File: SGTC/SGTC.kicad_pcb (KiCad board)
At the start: 2 copper layers, 110.5 x 62.6 mm, 9 parts, among them J1 Conn_01x08_Pin

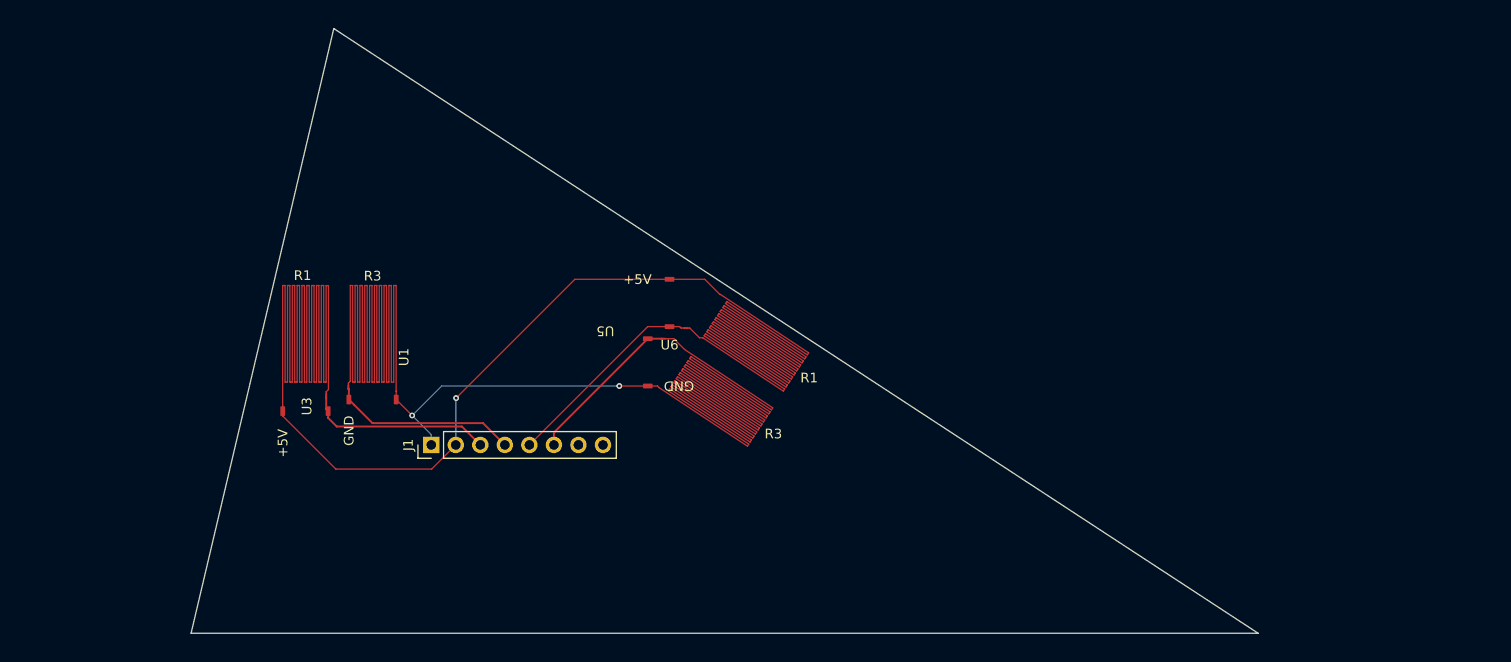
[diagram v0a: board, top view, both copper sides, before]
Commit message: fin center draft
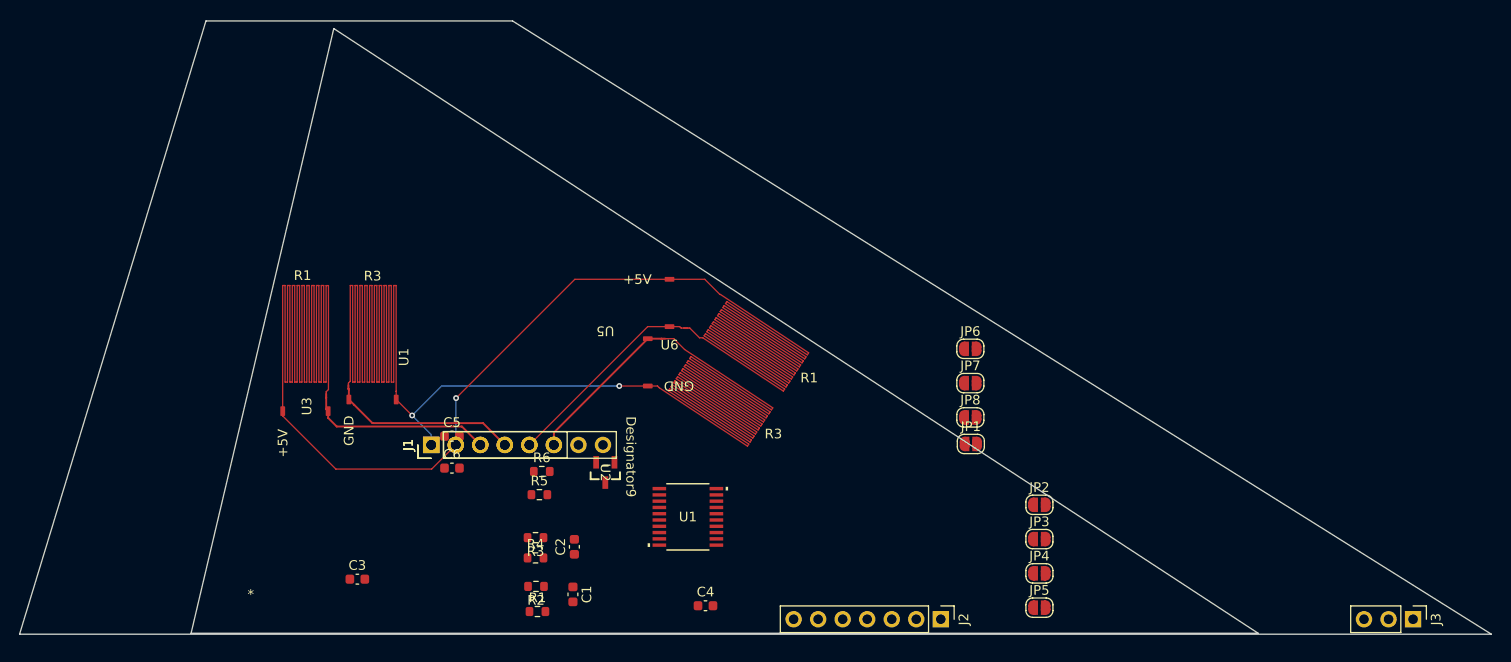
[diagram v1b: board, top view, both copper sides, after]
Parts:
- added C1: 10 nF, Capacitor_SMD:C_0603_1608Metric, F.Cu at (119.6, 120.8)
- added C2: 10 nF, Capacitor_SMD:C_0603_1608Metric, F.Cu at (119.8, 115.8)
- added C3: 10 nF, Capacitor_SMD:C_0603_1608Metric, F.Cu at (97.3, 119.2)
- added C4: 220 nF, Capacitor_SMD:C_0603_1608Metric, F.Cu at (133.3, 122.0)
- added C5: 1 uF, Capacitor_SMD:C_0603_1608Metric, F.Cu at (107.1, 104.4)
- added C6: 1 uF, Capacitor_SMD:C_0603_1608Metric, F.Cu at (107.1, 107.7)
- added J1: Conn_01x06_Pin, Connector_PinHeader_2.54mm:PinHeader_1x06_P2.54mm_Vertical, F.Cu at (104.9, 105.3)
- added J2: Conn_01x07_Pin, Connector_PinHeader_2.54mm:PinHeader_1x07_P2.54mm_Vertical, F.Cu at (157.7, 123.3)
- added J3: Conn_01x03_Pin, Connector_PinHeader_2.54mm:PinHeader_1x03_P2.54mm_Vertical, F.Cu at (206.6, 123.3)
- added JP1: SolderJumper_2_Open, Jumper:SolderJumper-2_P1.3mm_Open_RoundedPad1.0x1.5mm, F.Cu at (160.8, 105.2)
- added JP2: SolderJumper_2_Open, Jumper:SolderJumper-2_P1.3mm_Open_RoundedPad1.0x1.5mm, F.Cu at (167.9, 111.5)
- added JP3: SolderJumper_2_Open, Jumper:SolderJumper-2_P1.3mm_Open_RoundedPad1.0x1.5mm, F.Cu at (167.9, 115.0)
- added JP4: SolderJumper_2_Open, Jumper:SolderJumper-2_P1.3mm_Open_RoundedPad1.0x1.5mm, F.Cu at (167.9, 118.6)
- added JP5: SolderJumper_2_Open, Jumper:SolderJumper-2_P1.3mm_Open_RoundedPad1.0x1.5mm, F.Cu at (167.9, 122.2)
- added JP6: SolderJumper_2_Open, Jumper:SolderJumper-2_P1.3mm_Open_RoundedPad1.0x1.5mm, F.Cu at (160.8, 95.3)
- added JP7: SolderJumper_2_Open, Jumper:SolderJumper-2_P1.3mm_Open_RoundedPad1.0x1.5mm, F.Cu at (160.8, 98.9)
- added JP8: SolderJumper_2_Open, Jumper:SolderJumper-2_P1.3mm_Open_RoundedPad1.0x1.5mm, F.Cu at (160.8, 102.5)
- added R1: 10 k, Resistor_SMD:R_0603_1608Metric, F.Cu at (115.9, 122.5)
- added R2: 10 k, Resistor_SMD:R_0603_1608Metric, F.Cu at (115.8, 120.0)
- added R3: 10 k, Resistor_SMD:R_0603_1608Metric, F.Cu at (115.7, 114.9)
- added R4: 10 k, Resistor_SMD:R_0603_1608Metric, F.Cu at (115.7, 117.0)
- added R5: 10 k, Resistor_SMD:R_0603_1608Metric, F.Cu at (116.1, 110.5)
- added R6: 10 k, Resistor_SMD:R_0603_1608Metric, F.Cu at (116.4, 108.0)
- added U1: ADS131M03QPWRQ1, FinLib:ADS131M03, F.Cu at (131.5, 112.8)
- added U2: TMP235A4DBZR, FinLib:TMP235A4DBZR, F.Cu at (122.9, 108.2)
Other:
- board size 110.5 x 62.6 mm -> 152.4 x 63.5 mm

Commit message: strain gauge fix
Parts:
- removed C1, C2, C3: 10 nF, Capacitor_SMD:C_0603_1608Metric
- removed C4: 220 nF, Capacitor_SMD:C_0603_1608Metric
- removed C5, C6: 1 uF, Capacitor_SMD:C_0603_1608Metric
- removed J2: Conn_01x07_Pin, Connector_PinHeader_2.54mm:PinHeader_1x07_P2.54mm_Vertical
- removed J3: Conn_01x03_Pin, Connector_PinHeader_2.54mm:PinHeader_1x03_P2.54mm_Vertical
- removed JP1, JP2, JP3, JP4, JP5, JP6, JP7, JP8: SolderJumper_2_Open, Jumper:SolderJumper-2_P1.3mm_Open_RoundedPad1.0x1.5mm
- removed R1, R2, R3, R4, R5, R6: 10 k, Resistor_SMD:R_0603_1608Metric
- removed the REF** at (128.8, 94.3)
- removed the REF** at (96.3, 99.4)
- removed the REF** at (94.0, 100.3)
- removed the REF** at (131.2, 93.2)
- removed U1: ADS131M03QPWRQ1, FinLib:ADS131M03
- removed U1: ~, Library:StrainGaugeGND
- removed U2: TMP235A4DBZR, FinLib:TMP235A4DBZR
- removed the U5 at (127.3, 94.3)
- removed the U6 at (129.6, 95.5)
- added REF**: NetTie-2_SMD_Pad0.1mm, Library:NetTie-2_SMD_Pad0.1mm, F.Cu at (188.8, 87.7)
- added REF**: NetTie-2_SMD_Pad0.1mm, Library:NetTie-2_SMD_Pad0.1mm, F.Cu at (155.4, 91.8)
- added REF**: NetTie-2_SMD_Pad0.1mm, Library:NetTie-2_SMD_Pad0.1mm, F.Cu at (131.5, 93.6)
- added REF**: NetTie-2_SMD_Pad0.1mm, Library:NetTie-2_SMD_Pad0.1mm, F.Cu at (153.9, 93.4)
- added REF**: NetTie-2_SMD_Pad0.1mm, Library:NetTie-2_SMD_Pad0.1mm, F.Cu at (130.0, 95.2)
- added REF**: NetTie-2_SMD_Pad0.1mm, Library:NetTie-2_SMD_Pad0.1mm, F.Cu at (96.5, 99.3)
- added REF**: NetTie-2_SMD_Pad0.1mm, Library:NetTie-2_SMD_Pad0.1mm, F.Cu at (94.3, 99.3)
- added REF**: NetTie-2_SMD_Pad0.1mm, Library:NetTie-2_SMD_Pad0.1mm, F.Cu at (191.1, 87.7)
- added U3: ~, Library:StrainGaugeGND, F.Cu at (192.5, 86.1)
- added U5: ~, Library:StrainGaugeGND, F.Cu at (157.9, 92.2)
- added U5: ~, Library:StrainGaugeGND, F.Cu at (98.0, 100.9)
- added U5: ~, Library:StrainGaugeGND, F.Cu at (187.4, 86.1)
- added U5: ~, Library:StrainGaugeGND, F.Cu at (127.5, 94.8)
- added U6: ~, Library:StrainGaugeV, F.Cu at (154.3, 95.6)
- added U6: ~, Library:StrainGaugeV, F.Cu at (131.1, 91.4)
- J1: value Conn_01x08_Pin -> Conn_01x06_Pin; footprint Connector_PinHeader_2.54mm:PinHeader_1x08_P2.54mm_Vertical -> Connector_PinHeader_2.54mm:PinHeader_1x06_P2.54mm_Vertical
- U3: footprint Library:StrainGaugeV -> Library:StrainGaugeGND
- moved J1 79.1 mm to (180.5, 81.7), turned to -90 degrees
- moved U3 4.05 mm to (92.9, 100.8)
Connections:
- J1 pad 1: GAUGE1_IN_N -> A1_IN_N
- J1 pad 2: GAUGE1_IN_P -> A1_IN_P
- J1 pad 4: TMP_IN_N -> GND
- J1 pad 5: GAUGE2_IN_N -> A2_IN_N
- J1 pad 6: GAUGE2_IN_P -> A2_IN_P
- J1 pad 1: GND -> A1_IN_N
- J1 pad 2: +5V -> A1_IN_P
- J1 pad 3: A1_IN_P -> +3.3V
- J1 pad 4: A1_IN_N -> GND
- J1 pad 5: A2_IN_P -> A2_IN_N
- J1 pad 6: A2_IN_N -> A2_IN_P
- U3 pad 1: +5V -> +3.3V
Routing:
- net +3.3V: track 0.00 -> 934.7 mm
- net +5V: track 476.3 -> 0.00 mm, vias 1 -> 0
- net GND: track 448.8 -> 829.4 mm, vias 2 -> 0
- net A2_IN_N: track 16.4 -> 43.8 mm
- net A2_IN_P: track 21.1 -> 43.1 mm, vias 0 -> 2
- net A1_IN_P: track 19.1 -> 33.5 mm
- net A1_IN_N: track 19.2 -> 26.9 mm
- added copper zone on B.Cu, net GND
- added copper zone on F.Cu, net GND
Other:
- board size 152.4 x 63.5 mm -> 125.3 x 62.6 mm
- board text added: "R2"
- board text added: "R4"

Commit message: final version
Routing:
- net +3.3V: track 934.7 -> 935.3 mm
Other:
- outline, holes or cut-outs redrawn
